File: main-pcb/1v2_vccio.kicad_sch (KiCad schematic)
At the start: 1 part, among them U1 XC7S100-1FGGA484C

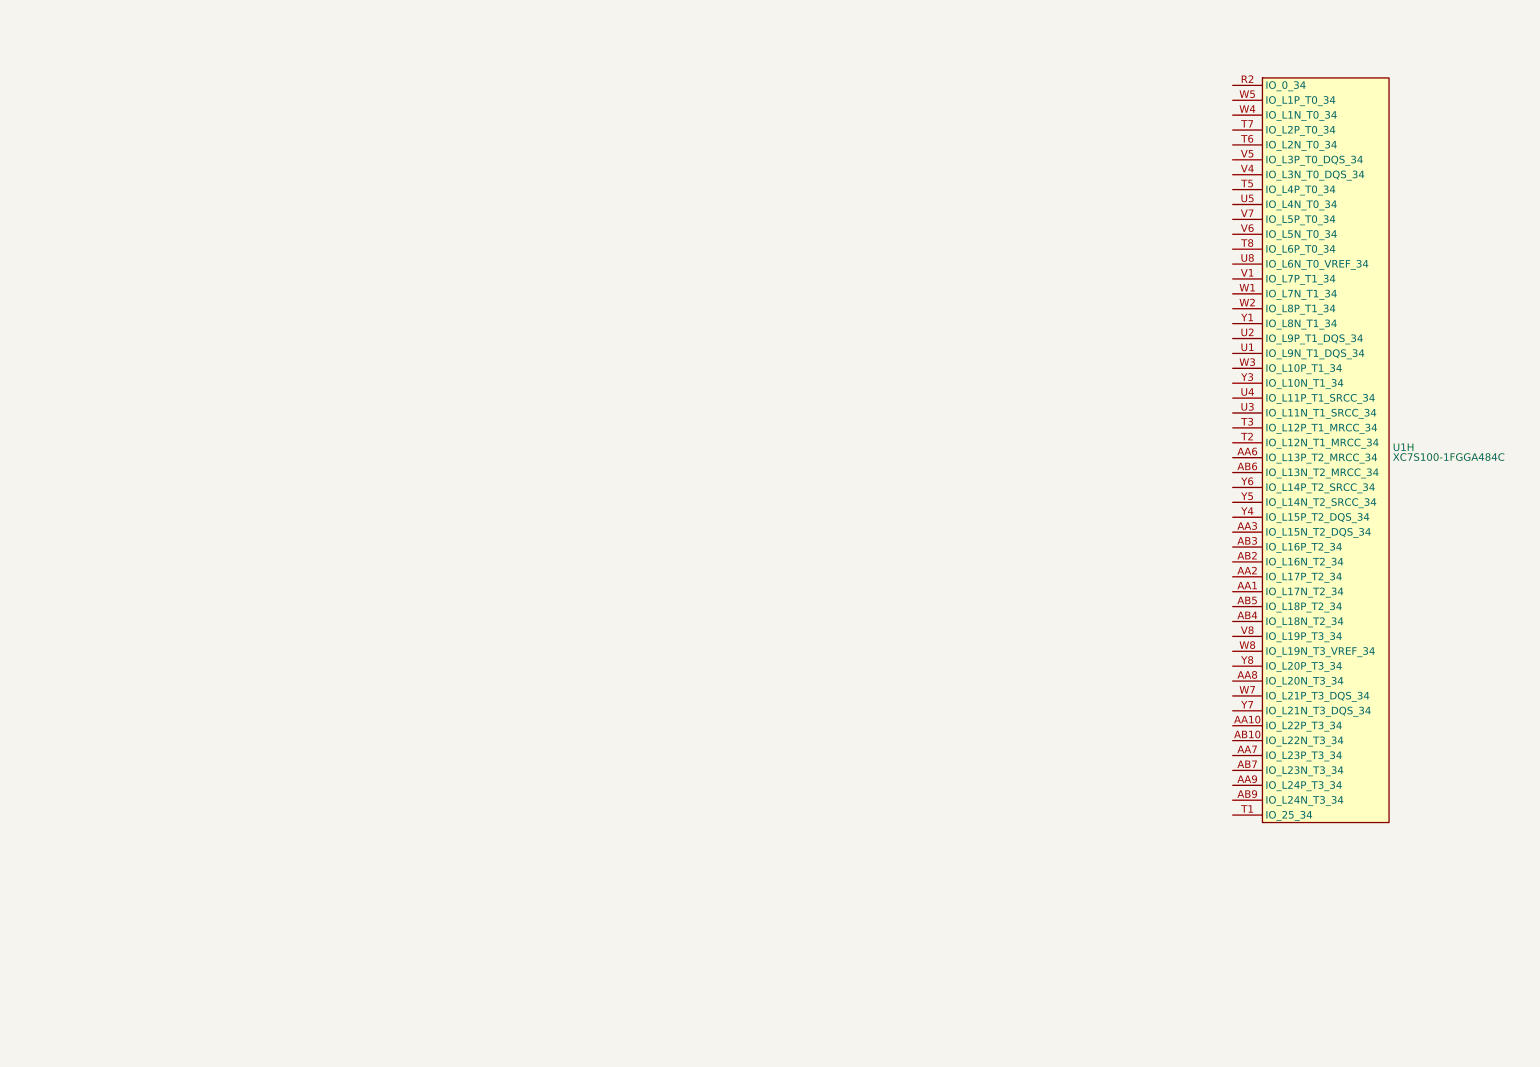
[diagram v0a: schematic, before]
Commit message: Initial design mostly done aside from USB connector, review, test points
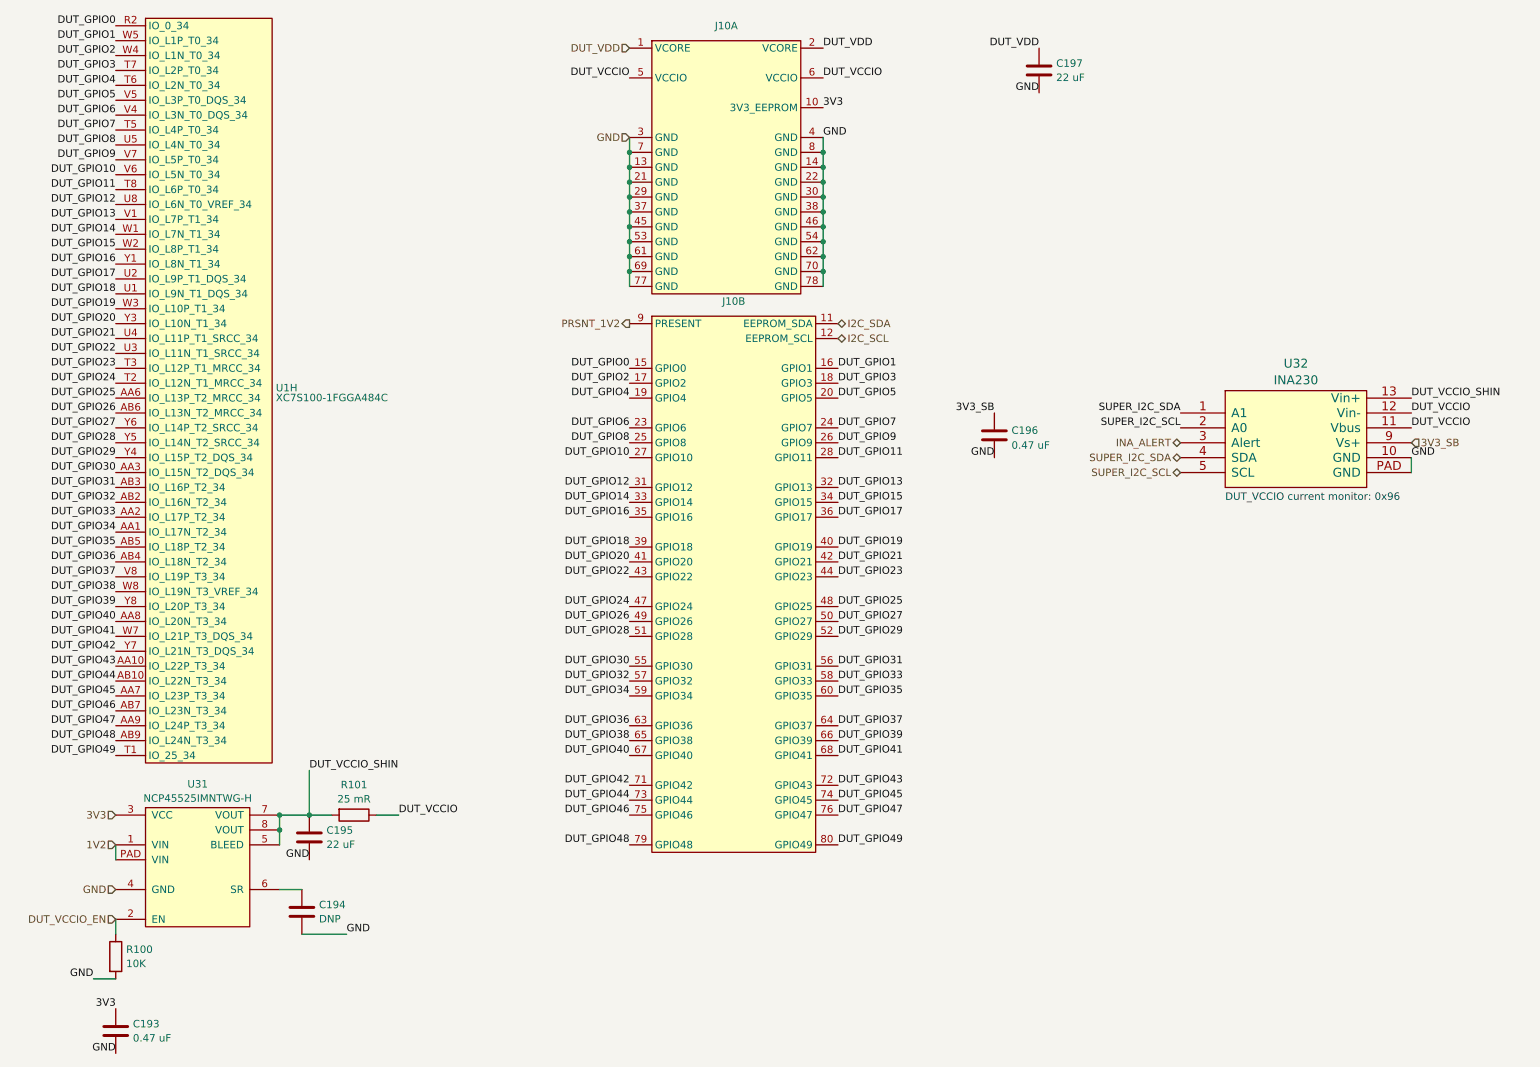
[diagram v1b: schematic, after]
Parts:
- added C193: 0.47 uF, symbol device:C
- added C194: DNP, symbol device:C
- added C195, C197: 22 uF, symbol device:C
- added C196: 0.47 uF, azonenberg_pcb:EIA_0402_CAP_NOSILK, symbol device:C
- added J10: ~, symbol special-azonenberg:CONN_DUMPTRUCK_HOST
- added R100: 10K, symbol device:R
- added R101: 25 mR, symbol passive-azonenberg:R_PWR
- added U31: NCP45525IMNTWG-H, symbol power-azonenberg:NCP45525
- added U32: INA230, azonenberg_pcb:QFN_16_0.5MM_3x3MM, symbol special-azonenberg:INA230
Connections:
- net DUT_GPIO34: now reaches U1.AA1 (IO_L17N_T2_34)
- net DUT_GPIO34: now also J10.59 (GPIO34)
- net DUT_GPIO43: now reaches U1.AA10 (IO_L22P_T3_34)
- net DUT_GPIO43: now also J10.72 (GPIO43)
- net DUT_GPIO33: now reaches U1.AA2 (IO_L17P_T2_34)
- net DUT_GPIO33: now also J10.58 (GPIO33)
- net DUT_GPIO30: now reaches U1.AA3 (IO_L15N_T2_DQS_34)
- net DUT_GPIO30: now also J10.55 (GPIO30)
- net DUT_GPIO25: now reaches U1.AA6 (IO_L13P_T2_MRCC_34)
- net DUT_GPIO25: now also J10.48 (GPIO25)
- net DUT_GPIO45: now reaches U1.AA7 (IO_L23P_T3_34)
- net DUT_GPIO45: now also J10.74 (GPIO45)
- net DUT_GPIO40: now reaches U1.AA8 (IO_L20N_T3_34)
- net DUT_GPIO40: now also J10.67 (GPIO40)
- net DUT_GPIO47: now reaches U1.AA9 (IO_L24P_T3_34)
- net DUT_GPIO47: now also J10.76 (GPIO47)
- net DUT_GPIO44: now reaches U1.AB10 (IO_L22N_T3_34)
- net DUT_GPIO44: now also J10.73 (GPIO44)
- net DUT_GPIO32: now reaches U1.AB2 (IO_L16N_T2_34)
- net DUT_GPIO32: now also J10.57 (GPIO32)
- net DUT_GPIO31: now reaches U1.AB3 (IO_L16P_T2_34)
- net DUT_GPIO31: now also J10.56 (GPIO31)
- net DUT_GPIO36: now reaches U1.AB4 (IO_L18N_T2_34)
- net DUT_GPIO36: now also J10.63 (GPIO36)
- net DUT_GPIO35: now reaches U1.AB5 (IO_L18P_T2_34)
- net DUT_GPIO35: now also J10.60 (GPIO35)
- net DUT_GPIO26: now reaches U1.AB6 (IO_L13N_T2_MRCC_34)
- net DUT_GPIO26: now also J10.49 (GPIO26)
- net DUT_GPIO46: now reaches U1.AB7 (IO_L23N_T3_34)
- net DUT_GPIO46: now also J10.75 (GPIO46)
- net DUT_GPIO48: now reaches U1.AB9 (IO_L24N_T3_34)
- net DUT_GPIO48: now also J10.79 (GPIO48)
- net DUT_GPIO0: now reaches U1.R2 (IO_0_34)
- net DUT_GPIO0: now also J10.15 (GPIO0)
- net DUT_GPIO49: now reaches U1.T1 (IO_25_34)
- net DUT_GPIO49: now also J10.80 (GPIO49)
- net DUT_GPIO24: now reaches U1.T2 (IO_L12N_T1_MRCC_34)
- net DUT_GPIO24: now also J10.47 (GPIO24)
- net DUT_GPIO23: now reaches U1.T3 (IO_L12P_T1_MRCC_34)
- net DUT_GPIO23: now also J10.44 (GPIO23)
- net DUT_GPIO7: now reaches U1.T5 (IO_L4P_T0_34)
- net DUT_GPIO7: now also J10.24 (GPIO7)
- net DUT_GPIO4: now reaches U1.T6 (IO_L2N_T0_34)
- net DUT_GPIO4: now also J10.19 (GPIO4)
- net DUT_GPIO3: now reaches U1.T7 (IO_L2P_T0_34)
- net DUT_GPIO3: now also J10.18 (GPIO3)
- net DUT_GPIO11: now reaches U1.T8 (IO_L6P_T0_34)
- net DUT_GPIO11: now also J10.28 (GPIO11)
- net DUT_GPIO18: now reaches U1.U1 (IO_L9N_T1_DQS_34)
- net DUT_GPIO18: now also J10.39 (GPIO18)
- net DUT_GPIO17: now reaches U1.U2 (IO_L9P_T1_DQS_34)
- net DUT_GPIO17: now also J10.36 (GPIO17)
- net DUT_GPIO22: now reaches U1.U3 (IO_L11N_T1_SRCC_34)
- net DUT_GPIO22: now also J10.43 (GPIO22)
- net DUT_GPIO21: now reaches U1.U4 (IO_L11P_T1_SRCC_34)
- net DUT_GPIO21: now also J10.42 (GPIO21)
- net DUT_GPIO8: now reaches U1.U5 (IO_L4N_T0_34)
- net DUT_GPIO8: now also J10.25 (GPIO8)
- net DUT_GPIO12: now reaches U1.U8 (IO_L6N_T0_VREF_34)
- net DUT_GPIO12: now also J10.31 (GPIO12)
- net DUT_GPIO13: now reaches U1.V1 (IO_L7P_T1_34)
- net DUT_GPIO13: now also J10.32 (GPIO13)
- net DUT_GPIO6: now reaches U1.V4 (IO_L3N_T0_DQS_34)
- net DUT_GPIO6: now also J10.23 (GPIO6)
- net DUT_GPIO5: now reaches U1.V5 (IO_L3P_T0_DQS_34)
- net DUT_GPIO5: now also J10.20 (GPIO5)
- net DUT_GPIO10: now reaches U1.V6 (IO_L5N_T0_34)
- net DUT_GPIO10: now also J10.27 (GPIO10)
- net DUT_GPIO9: now reaches U1.V7 (IO_L5P_T0_34)
- net DUT_GPIO9: now also J10.26 (GPIO9)
- net DUT_GPIO37: now reaches U1.V8 (IO_L19P_T3_34)
- net DUT_GPIO37: now also J10.64 (GPIO37)
- net DUT_GPIO14: now reaches U1.W1 (IO_L7N_T1_34)
- net DUT_GPIO14: now also J10.33 (GPIO14)
- net DUT_GPIO15: now reaches U1.W2 (IO_L8P_T1_34)
- net DUT_GPIO15: now also J10.34 (GPIO15)
- net DUT_GPIO19: now reaches U1.W3 (IO_L10P_T1_34)
- net DUT_GPIO19: now also J10.40 (GPIO19)
- net DUT_GPIO2: now reaches U1.W4 (IO_L1N_T0_34)
- net DUT_GPIO2: now also J10.17 (GPIO2)
- net DUT_GPIO1: now reaches U1.W5 (IO_L1P_T0_34)
- net DUT_GPIO1: now also J10.16 (GPIO1)
- net DUT_GPIO41: now reaches U1.W7 (IO_L21P_T3_DQS_34)
- net DUT_GPIO41: now also J10.68 (GPIO41)
- net DUT_GPIO38: now reaches U1.W8 (IO_L19N_T3_VREF_34)
- net DUT_GPIO38: now also J10.65 (GPIO38)
- net DUT_GPIO16: now reaches U1.Y1 (IO_L8N_T1_34)
- net DUT_GPIO16: now also J10.35 (GPIO16)
- net DUT_GPIO20: now reaches U1.Y3 (IO_L10N_T1_34)
- net DUT_GPIO20: now also J10.41 (GPIO20)
- net DUT_GPIO29: now reaches U1.Y4 (IO_L15P_T2_DQS_34)
- net DUT_GPIO29: now also J10.52 (GPIO29)
- net DUT_GPIO28: now reaches U1.Y5 (IO_L14N_T2_SRCC_34)
- net DUT_GPIO28: now also J10.51 (GPIO28)
- net DUT_GPIO27: now reaches U1.Y6 (IO_L14P_T2_SRCC_34)
- net DUT_GPIO27: now also J10.50 (GPIO27)
- net DUT_GPIO42: now reaches U1.Y7 (IO_L21N_T3_DQS_34)
- net DUT_GPIO42: now also J10.71 (GPIO42)
- net DUT_GPIO39: now reaches U1.Y8 (IO_L20P_T3_34)
- net DUT_GPIO39: now also J10.66 (GPIO39)
- new net: C194.1, U31.6 (SR)
- new net 1V2: U31.1 (VIN), U31.PAD (VIN)
- new net 3V3: C193.1, J10.10 (3V3_EEPROM), U31.3 (VCC)
- new net 3V3_SB: C196.1, U32.9 (Vs+)
- new net DUT_VCCIO: J10.5 (VCCIO), J10.6 (VCCIO), R101.1, U32.11 (Vbus), U32.12 (Vin-)
- new net DUT_VCCIO_EN: R100.1, U31.2 (EN)
- new net DUT_VCCIO_SHIN: C195.1, R101.2, U31.5 (BLEED), U31.7 (VOUT), U31.8 (VOUT), U32.13 (Vin+)
- new net DUT_VDD: C197.1, J10.1 (VCORE), J10.2 (VCORE)
- new net GND: C193.2, C194.2, C195.2, C196.2, C197.2, J10.13 (GND), J10.14 (GND), J10.21 (GND), J10.22 (GND), J10.29 (GND), J10.3 (GND), J10.30 (GND), J10.37 (GND), J10.38 (GND), J10.4 (GND), J10.45 (GND), J10.46 (GND), J10.53 (GND), J10.54 (GND), J10.61 (GND), J10.62 (GND), J10.69 (GND), J10.7 (GND), J10.70 (GND), J10.77 (GND), J10.78 (GND), J10.8 (GND), R100.2, U31.4 (GND), U32.10 (GND), U32.PAD (GND)
- new net I2C_SCL: J10.12 (EEPROM_SCL)
- new net I2C_SDA: J10.11 (EEPROM_SDA)
- new net INA_ALERT: U32.3 (Alert)
- new net PRSNT_1V2: J10.9 (PRESENT)
- new net SUPER_I2C_SCL: U32.2 (A0), U32.5 (SCL)
- new net SUPER_I2C_SDA: U32.1 (A1), U32.4 (SDA)
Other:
- note added: "DUT_VCCIO current monitor: 0x96"
- moved on the sheet: U1H

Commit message: More schematic tweaks and test points
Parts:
- C193, C194: footprint (none) -> azonenberg_pcb:EIA_0402_CAP_NOSILK
- J10: value ~ -> CONN_DUMPTRUCK_HOST
- R100, R101: footprint (none) -> azonenberg_pcb:EIA_0402_RES_NOSILK
- U31: footprint (none) -> azonenberg_pcb:DFN_8_0.5MM_2x2MM
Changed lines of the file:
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@@
 			)
 		)
-		(property "Footprint" ""
+		(property "Footprint" "azonenberg_pcb:EIA_0402_CAP_NOSILK"
 			(at 47.9552 194.31 0)
 			(effects
@@
 			)
 		)
-		(property "Value" "~"
+		(property "Value" "CONN_DUMPTRUCK_HOST"
 			(at 152.4 67.7299 0)
 			(effects
@@
 			)
 		)
-		(property "Footprint" ""
+		(property "Footprint" "azonenberg_pcb:DFN_8_0.5MM_2x2MM"
 			(at 52.07 172.72 0)
 			(effects
@@
 			)
 		)
-		(property "Value" "~"
+		(property "Value" "CONN_DUMPTRUCK_HOST"
 			(at 151.13 20.7399 0)
 			(effects
@@
 			)
 		)
-		(property "Footprint" ""
+		(property "Footprint" "azonenberg_pcb:EIA_0402_RES_NOSILK"
 			(at 87.63 151.892 90)
 			(effects
@@
 			)
 		)
-		(property "Footprint" ""
+		(property "Footprint" "azonenberg_pcb:EIA_0402_CAP_NOSILK"
 			(at 79.7052 173.99 0)
 			(effects
@@
 			)
 		)
-		(property "Footprint" ""
+		(property "Footprint" "azonenberg_pcb:EIA_0402_RES_NOSILK"
 			(at 45.212 177.8 90)
 			(effects

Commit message: Added some RGB LEDs, changed a few voltage dividers to match what was in stock. Time for next round of review.
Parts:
- C195: footprint (none) -> azonenberg_pcb:EIA_0805_CAP_NOSILK
- C197: footprint (none) -> azonenberg_pcb:EIA_1206_CAP_NOSILK
- J10: footprint (none) -> azonenberg_pcb:CONN_SAMTEC_BTE-040-01-F-D-A-K
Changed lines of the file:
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@@
 	(title_block
 		(title "DUMPTRUCK flash dumper")
-		(date "2024-10-16")
+		(date "2024-10-17")
 		(rev "0.1")
 		(company "Antikernel Labs")
@@
 			)
 		)
-		(property "Footprint" ""
+		(property "Footprint" "azonenberg_pcb:CONN_SAMTEC_BTE-040-01-F-D-A-K"
 			(at 138.43 160.02 0)
 			(effects
@@
 			)
 		)
-		(property "Footprint" ""
+		(property "Footprint" "azonenberg_pcb:EIA_1206_CAP_NOSILK"
 			(at 205.4352 30.48 0)
 			(effects
@@
 			)
 		)
-		(property "Footprint" ""
+		(property "Footprint" "azonenberg_pcb:CONN_SAMTEC_BTE-040-01-F-D-A-K"
 			(at 138.43 64.77 0)
 			(effects
@@
 			)
 		)
-		(property "Footprint" ""
+		(property "Footprint" "azonenberg_pcb:EIA_0805_CAP_NOSILK"
 			(at 80.9752 161.29 0)
 			(effects

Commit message: Finished schematic review
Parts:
- R100: value 10K -> DNP
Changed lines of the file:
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@@
 			)
 		)
-		(property "Value" "10K"
+		(property "Value" "DNP"
 			(at 48.768 179.0121 0)
 			(effects
